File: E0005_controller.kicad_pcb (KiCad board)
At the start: 4 copper layers, 125 x 65 mm, 270 parts, among them J1 SM04B-GHS-TB, J10 FH12-18S-0.5SH, J11 USB4105-GF-A, J12 SM02B-GHS-TB, J2 SM04B-GHS-TB, J3 SM04B-GHS-TB, J4 SM04B-GHS-TB, J5 SM06B-GHS-TB, J6 SM02B-GHS-TB, J7 SM02B-GHS-TB, J8 SM02B-GHS-TB, J9 SM02B-GHS-TB, Q1 PSMN2R0-30YLDX, Q11 2N7002, Q12 2N7002, Q13 AO3401A, Q14 2N7002, Q2 PSMN2R0-30YLDX, Q3 2N7002, Q4 2N7002, Q5 2N7002, Q6 2N7002, Q7 2N7002, SW1 PWR, SW2 BOOT, SW3 RESET, U1 ESP32-S3-WROOM-1-N16R2, U10 TPS259470ARPW, U11 TPS259470ARPW, U12 TPS259470ARPW, U13 TPS259470ARPW, U14 TPS259470ARPW, U15 MAX17205G+, U16 TPS259470ARPW, U17 TPS56637RPAR, U2 BQ25887RGER, U4 USBLC6-2SC6, U5 TPS629210DRL, U6 S-8252AAG-M6T1U, U8 PCA9548APW, U9 TCA9535PWR

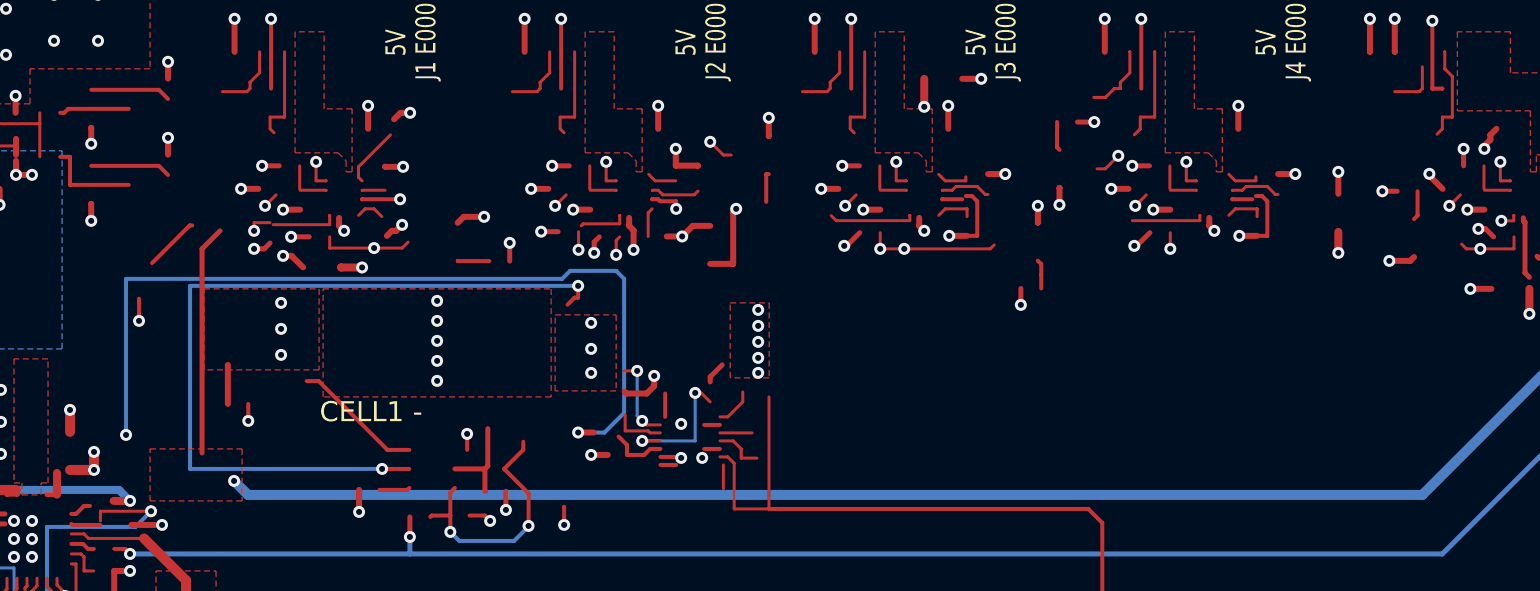
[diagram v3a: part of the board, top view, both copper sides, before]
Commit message: E0005 routing: U8/U9 fan-out, CHG_G/BAT+ reroute, In2 V5 band narrowed (top In2 strip free for signals)
Co-Authored-By: Claude Opus 5.5 <noreply@anthropic.com>
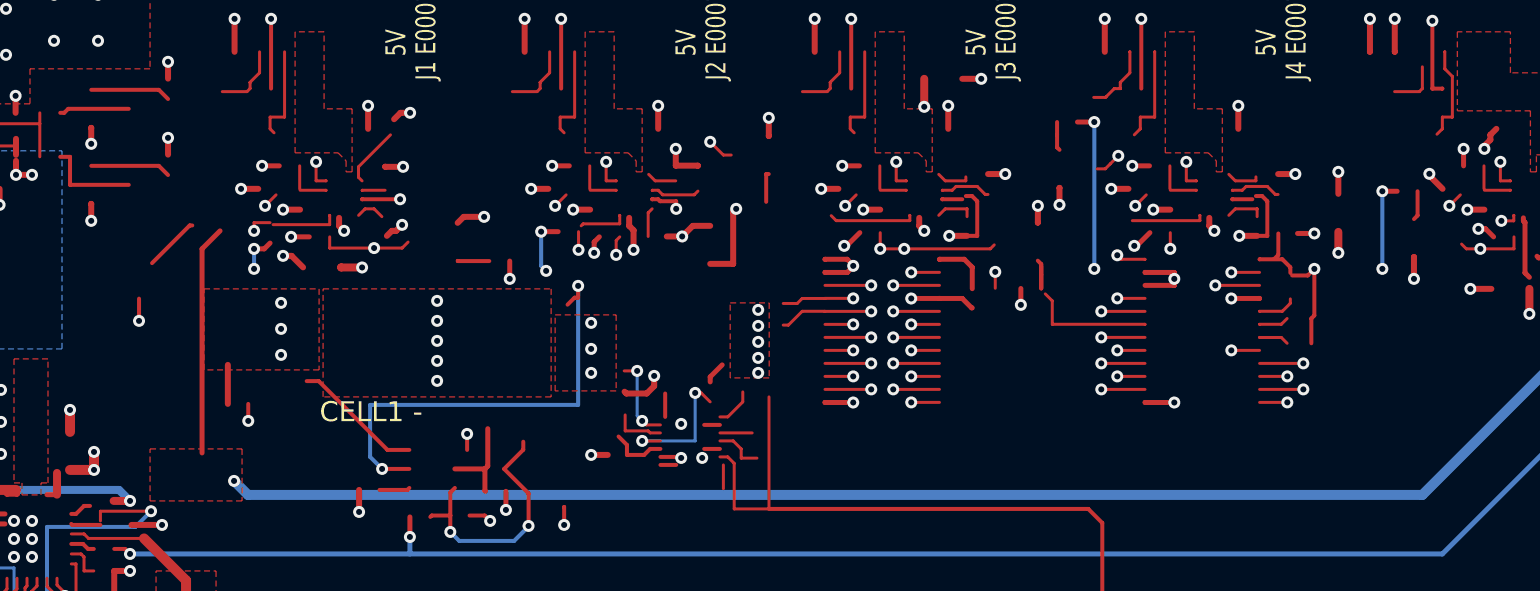
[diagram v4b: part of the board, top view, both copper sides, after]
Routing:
- net BAT+: track 69.9 -> 26.7 mm, vias 10 -> 8
- net +3V3: track 43.1 -> 68.6 mm, vias 15 -> 20
- net /Battery pack, protection, gauge/CHG_G: track 40.8 -> 22.4 mm
- net GND: track 136.2 -> 151.0 mm, vias 102 -> 109
- net /I2C mux, expander, 5 V peripheral ports/PORT3_OFF: track 1.46 -> 8.90 mm
- net /I2C mux, expander, 5 V peripheral ports/PORT1_SCL: track 0.00 -> 4.69 mm, vias 0 -> 1
- net /I2C mux, expander, 5 V peripheral ports/PORT1_SDA: track 0.00 -> 3.61 mm, vias 0 -> 1
- net MUX_RST_N: track 0.00 -> 2.31 mm, vias 0 -> 1
- net LCD_SCL: track 0.00 -> 2.31 mm, vias 0 -> 1
- net I2C1_SCL: track 0.00 -> 2.31 mm, vias 0 -> 1
- net /I2C mux, expander, 5 V peripheral ports/PORT5_SCL: track 0.00 -> 2.31 mm, vias 0 -> 1
- net /I2C mux, expander, 5 V peripheral ports/PORT4_SCL: track 0.00 -> 2.31 mm, vias 0 -> 1
- net /I2C mux, expander, 5 V peripheral ports/PORT3_SCL: track 0.00 -> 2.31 mm, vias 0 -> 1
- net /I2C mux, expander, 5 V peripheral ports/PORT2_SCL: track 0.00 -> 2.31 mm, vias 0 -> 1
- net /I2C mux, expander, 5 V peripheral ports/MUX7_SCL: track 0.00 -> 2.31 mm, vias 0 -> 1
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
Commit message: E0005 routing: U8 pull-up network, 3V3 rail, port fan-out fixes
Co-Authored-By: Claude Opus 5.5 <noreply@anthropic.com>
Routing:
- net +3V3: track 68.6 -> 100.0 mm, vias 20 -> 32
- net /I2C mux, expander, 5 V peripheral ports/PORT2_SCL: track 2.31 -> 10.2 mm, vias 1 -> 2
- net /I2C mux, expander, 5 V peripheral ports/PORT2_SDA: track 1.41 -> 9.29 mm, vias 1 -> 2
- net /I2C mux, expander, 5 V peripheral ports/PORT4_SCL: track 2.31 -> 9.00 mm, vias 1 -> 2
- net /I2C mux, expander, 5 V peripheral ports/PORT3_SDA: track 1.41 -> 7.93 mm, vias 1 -> 2
- net /I2C mux, expander, 5 V peripheral ports/PORT4_SDA: track 1.41 -> 7.39 mm, vias 1 -> 2
- net /I2C mux, expander, 5 V peripheral ports/PORT3_SCL: track 2.31 -> 7.07 mm, vias 1 -> 2
- net /I2C mux, expander, 5 V peripheral ports/PORT3_OFF: track 8.90 -> 7.77 mm

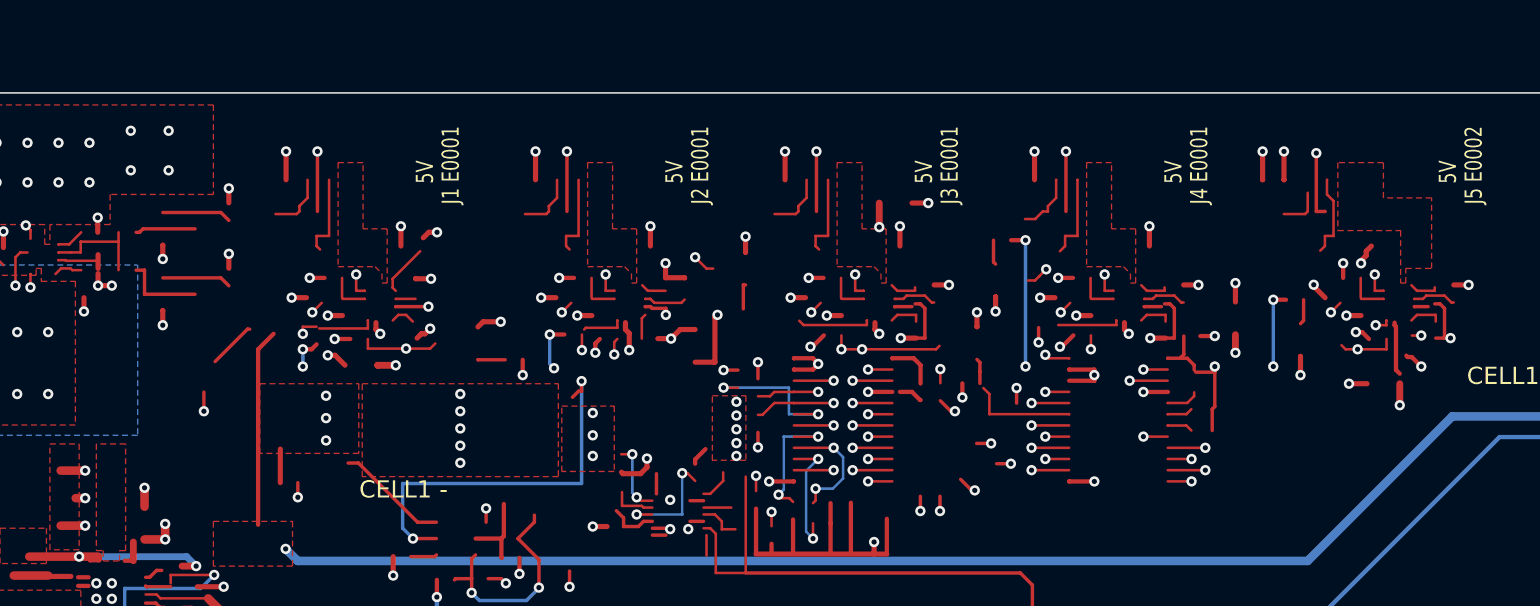
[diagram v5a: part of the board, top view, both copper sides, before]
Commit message: E0005 routing WIP: port 1/2 I2C to U8, MUX6/7 pull-ups, V5 top bus for ports 4/5, probe/grid helpers
Co-Authored-By: Claude Opus 5.5 <noreply@anthropic.com>
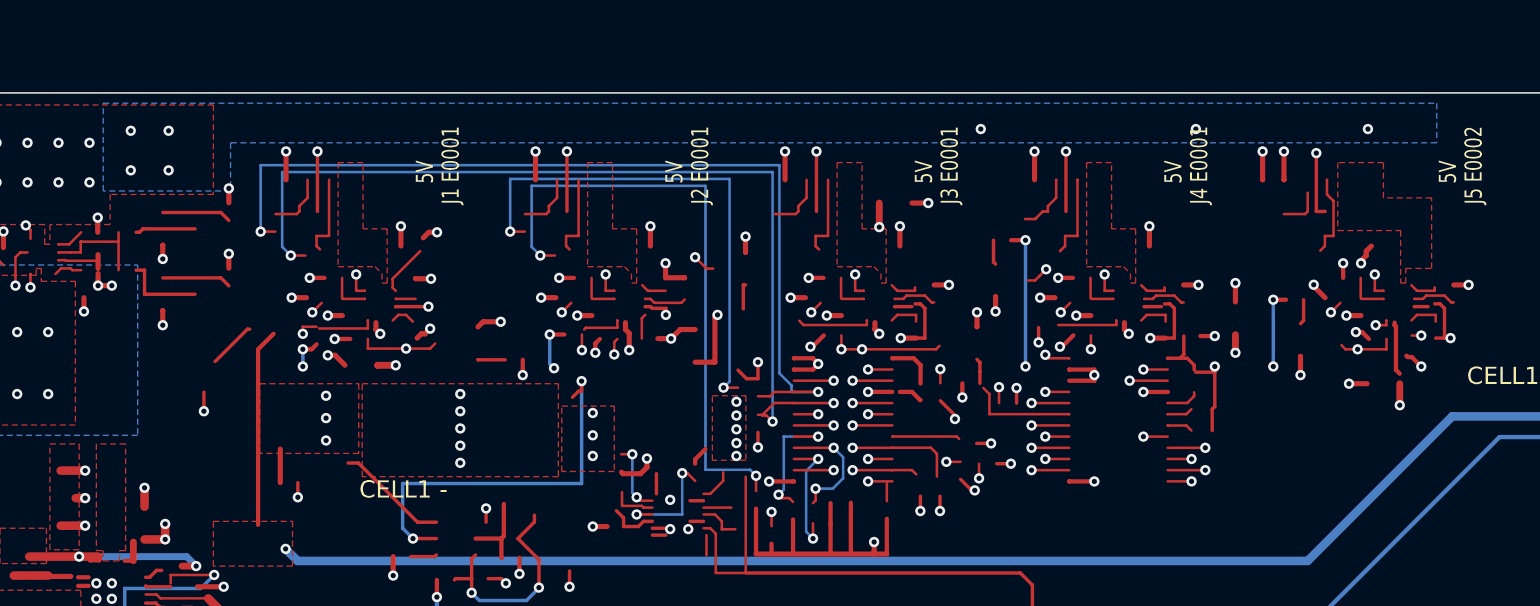
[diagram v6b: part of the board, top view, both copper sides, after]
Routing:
- net /I2C mux, expander, 5 V peripheral ports/PORT1_SDA: track 3.61 -> 53.5 mm, vias 1 -> 2
- net /I2C mux, expander, 5 V peripheral ports/PORT1_SCL: track 4.69 -> 54.3 mm, vias 1 -> 3
- net /I2C mux, expander, 5 V peripheral ports/PORT2_SCL: track 10.2 -> 45.0 mm, vias 2 -> 3
- net /I2C mux, expander, 5 V peripheral ports/PORT2_SDA: track 9.29 -> 37.3 mm, vias 2 -> 3
- net /I2C mux, expander, 5 V peripheral ports/MUX7_SCL: track 2.31 -> 13.0 mm, vias 1 -> 2
- net /I2C mux, expander, 5 V peripheral ports/MUX7_SDA: track 1.41 -> 10.7 mm, vias 1 -> 2
- net /I2C mux, expander, 5 V peripheral ports/MUX6_SCL: track 2.31 -> 10.1 mm, vias 1 -> 2
- net LCD_SCL: track 2.31 -> 6.38 mm
- net /I2C mux, expander, 5 V peripheral ports/MUX6_SDA: track 1.41 -> 3.94 mm, vias 1 -> 0
- net /I2C mux, expander, 5 V peripheral ports/PORT5_SCL: track 2.31 -> 3.81 mm
- net /I2C mux, expander, 5 V peripheral ports/PORT5_SDA: track 1.41 -> 2.44 mm
- net +3V3: track 100.0 -> 100.8 mm, vias 32 -> 31
- net V5: vias 39 -> 42
- added copper zone on B.Cu, net V5

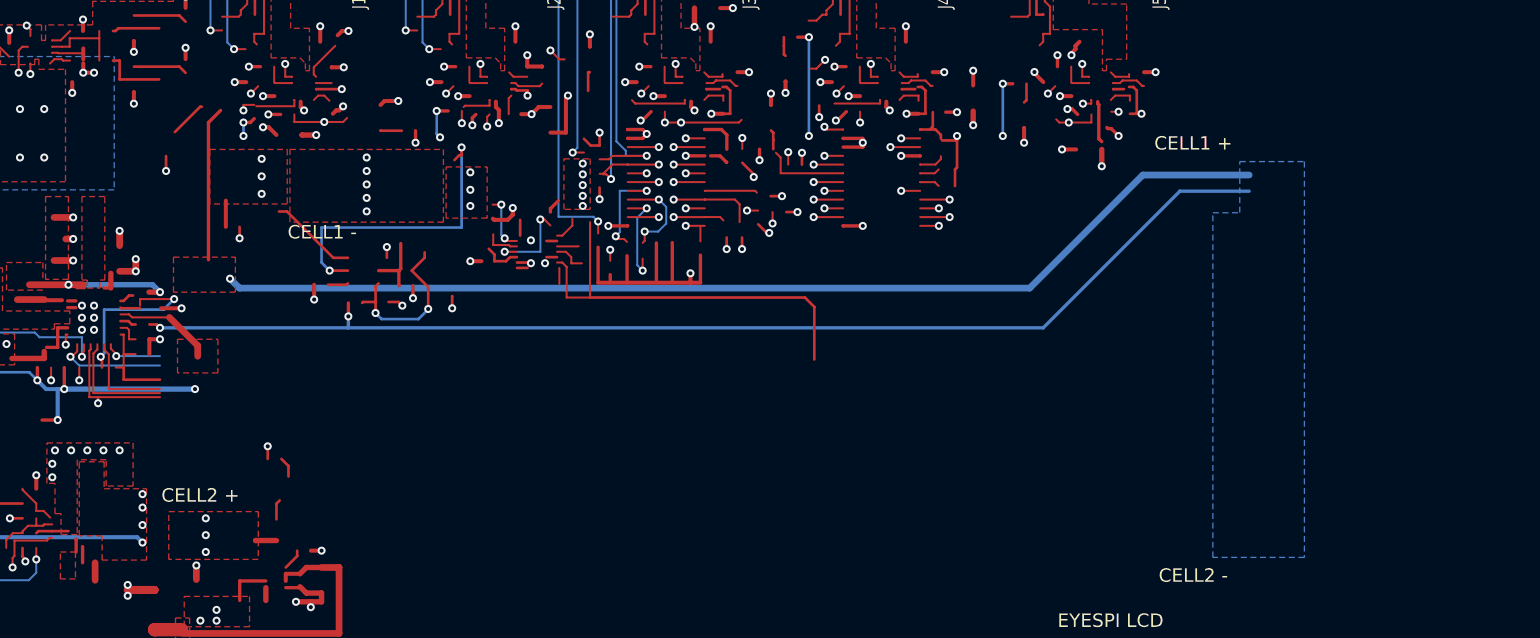
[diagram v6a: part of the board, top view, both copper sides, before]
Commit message: E0005 routing: U1 north pin-row cluster (pull-ups, sense dividers, SW RC), USB D+/D- 90 ohm pair (W0.19/S0.20, skew <0.01 mm), MID pour cut back east of BH1 lug for y<-9
Co-Authored-By: Claude Opus 5.5 <noreply@anthropic.com>
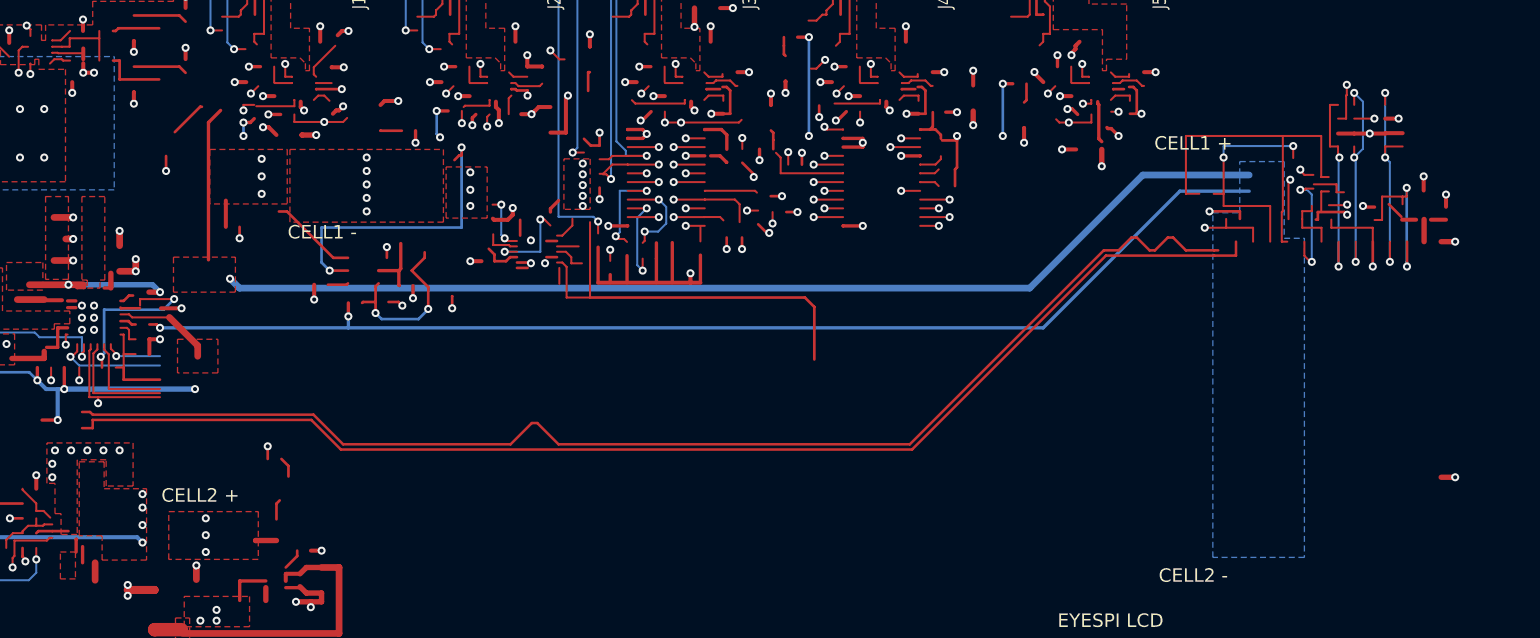
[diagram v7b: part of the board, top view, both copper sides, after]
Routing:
- net USB_DP: track 0.00 -> 94.2 mm
- net USB_DN: track 0.00 -> 94.2 mm
- net /MCU, UI, LCD, switches/SW3: track 0.00 -> 27.2 mm
- net /MCU, UI, LCD, switches/SW4: track 0.00 -> 17.4 mm, vias 0 -> 2
- net V5_SENSE: track 0.00 -> 17.2 mm, vias 0 -> 3
- net CC1_SENSE: track 0.00 -> 16.3 mm, vias 0 -> 3
- net CC2_SENSE: track 0.00 -> 15.1 mm, vias 0 -> 2
- net /MCU, UI, LCD, switches/EN: track 0.00 -> 13.1 mm, vias 0 -> 2
- net +3V3: track 100.8 -> 113.8 mm, vias 31 -> 33
- net /MCU, UI, LCD, switches/SW2: track 0.00 -> 11.6 mm, vias 0 -> 2
- net GND: track 150.6 -> 160.3 mm, vias 109 -> 115
- net CHG_INT_N: track 4.30 -> 10.9 mm, vias 1 -> 2
- net I2C0_SDA: track 10.1 -> 15.4 mm, vias 1 -> 2
- net /MCU, UI, LCD, switches/SW1: track 0.00 -> 4.79 mm
- net /Power: USB-C, U_IN, charger, 5 V buck, 3V3/CC2: track 0.00 -> 3.13 mm, vias 0 -> 1
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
